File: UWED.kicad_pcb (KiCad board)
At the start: 2 copper layers, 34 x 49.5 mm, 52 parts, among them U1 RFD22301

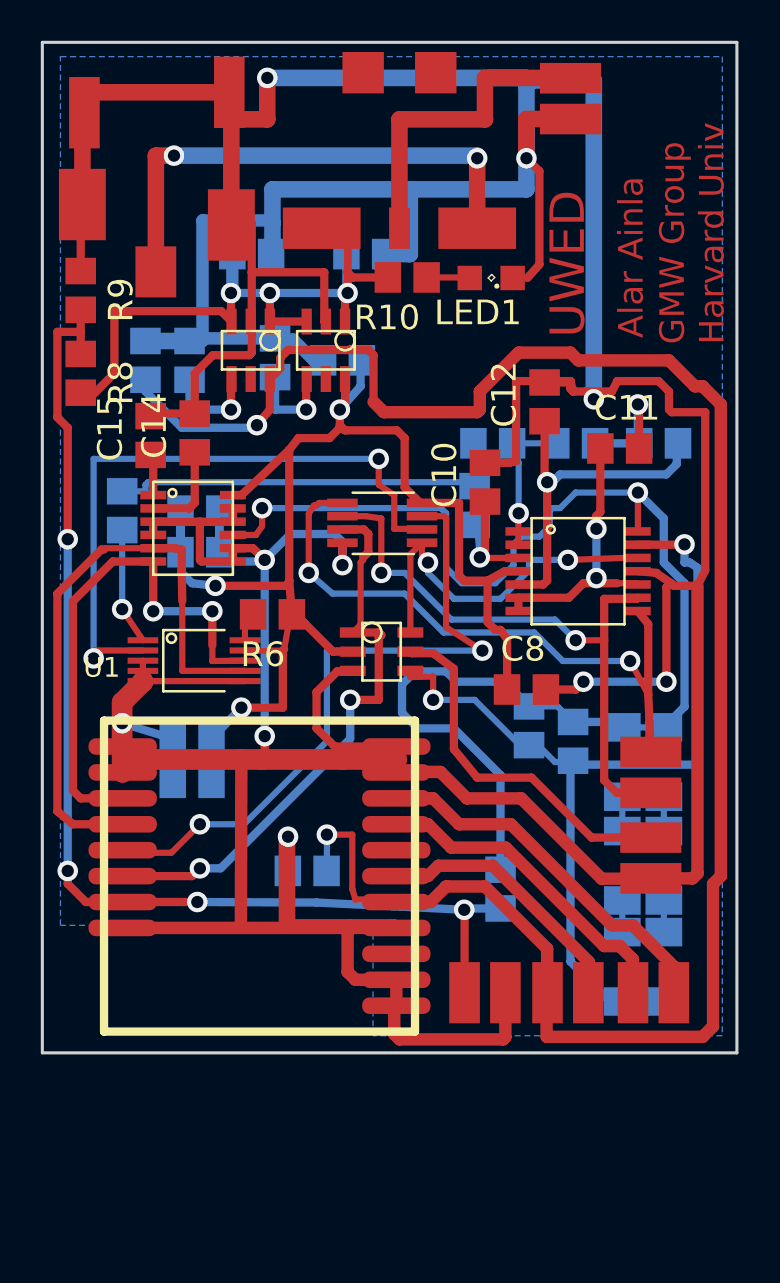
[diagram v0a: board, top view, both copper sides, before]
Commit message: New project files with ESP-WROOM-32 and integrated charger chip - untested.
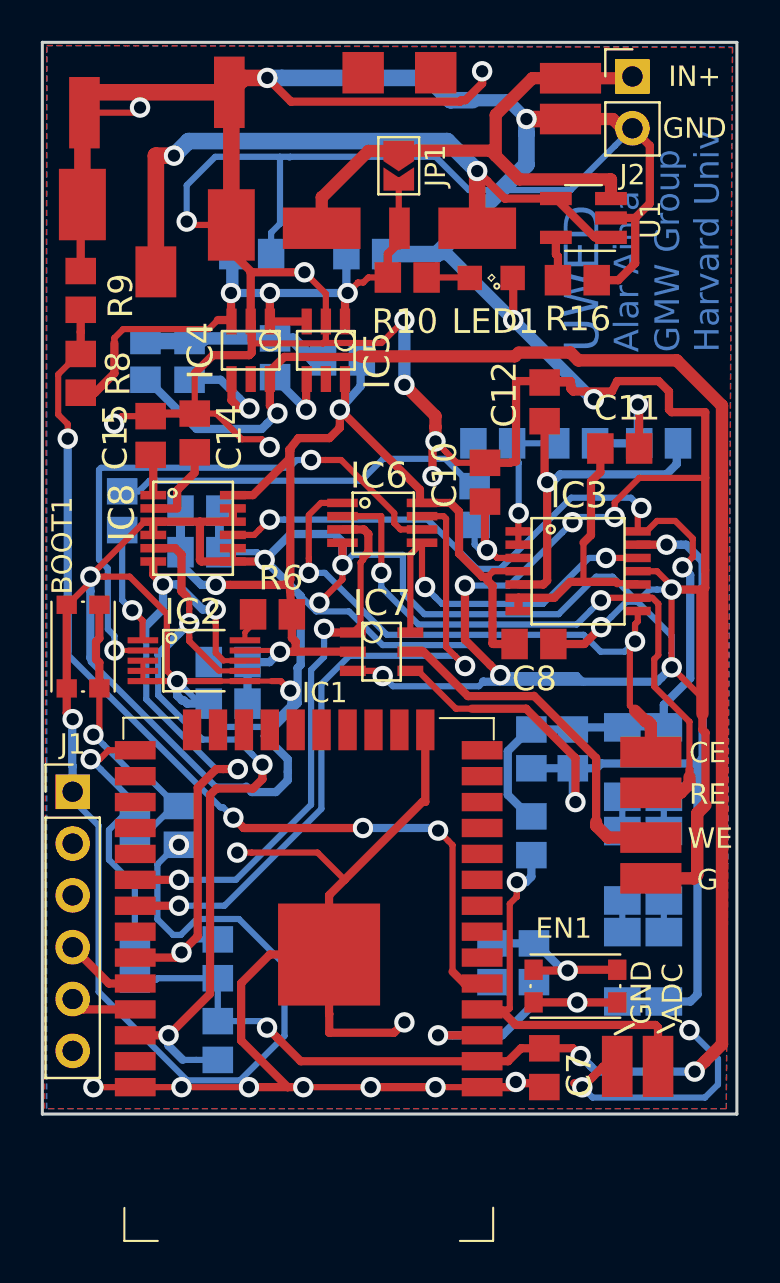
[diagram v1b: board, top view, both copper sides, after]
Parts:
- removed U$1: 4OPAMPS-AD8608ARUZ, UWED:MSOP14_0.65MM
- removed U$10, U$11: LDO-MIC5205-3.3YM5-TR, UWED:SOT-23-6
- removed U$12: SWITCH_MAX4643EUA, UWED:MSOP8_0.65MM
- removed U$13: SWITCH_MAX4644EUT, UWED:SOT-23-6
- removed U$14: SW_TOGGLELARGE, UWED:TOGGLE_34E
- removed U$2: ADC_LTC2471IMS, UWED:MSOP12_0.65MM
- removed U$4, U$5: CONTACT_PADS_SMD_2, UWED:CONTACT_PADS_SMD_2
- removed U$8: DAC_AD5667RBRMZ-2, UWED:MSOP10_0.5MM
- removed U$9: DC_JACK_0.7MM, UWED:PJ-032H-SMT
- added BOOT1: KMR221G LFS, Buttons_Switches_SMD:SW_SPST_KMR2, F.Cu at (133.5, 109.9)
- added C20: 1n, UWED:C0805, B.Cu at (138.2, 118.6)
- added C21: 1n, UWED:C0805, B.Cu at (153.5, 125.3)
- added EN1: KMR221G LFS, Buttons_Switches_SMD:SW_SPST_KMR2, F.Cu at (157.6, 126.5)
- added IC1: ESP32-WROOM-32, digikey-footprints:ESP32-WROOM-32D, F.Cu at (144.5, 123.2)
- added IC2: DAC_AD5667RBRMZ-2, UWED:MSOP10_0.5MM, F.Cu at (136.4, 109.5)
- added IC3: 4OPAMPS-AD8608ARUZ, UWED:MSOP14_0.65MM, F.Cu at (155.5, 104.2)
- added IC4: LDO-MIC5205-3.3YM5-TR, UWED:SOT-23-6, F.Cu at (142.6, 93.9)
- added IC5: LDO-MIC5205-3.3YM5-TR, UWED:SOT-23-6, F.Cu at (146.3, 93.9)
- added IC6: SWITCH_MAX4643EUA, UWED:MSOP8_0.65MM, F.Cu at (146.2, 102.8)
- added IC7: SWITCH_MAX4644EUT, UWED:SOT-23-6, F.Cu at (146.7, 109.2)
- added IC8: ADC_LTC2471IMS, UWED:MSOP12_0.65MM, F.Cu at (136.9, 102.4)
- added J1: DNP, Pin_Headers:Pin_Header_Straight_1x06_Pitch2.54mm, F.Cu at (133.0, 117.0)
- added J2: DNP, Pin_Headers:Pin_Header_Straight_1x02_Pitch2.54mm, F.Cu at (160.4, 81.9)
- added JP1: Jumper_2_Open, Jumper:SolderJumper-2_P1.3mm_Open_TrianglePad1.0x1.5mm, F.Cu at (148.9, 86.3)
- added P1: PJ-032H-SMT-TR, UWED:PJ-032H-SMT, F.Cu at (137.0, 79.2)
- added P2: 34EWMSP12M6RT, UWED:TOGGLE_34E, F.Cu at (147.2, 81.7)
- added R11: 10k, UWED:R0805, B.Cu at (140.1, 125.2)
- added R12: 10k, UWED:R0805, B.Cu at (140.1, 129.2)
- added R13: 100k, UWED:R0805, B.Cu at (136.0, 125.2)
- added R14: 470R, UWED:R0805, B.Cu at (136.0, 118.6)
- added R15: 470R, UWED:R0805, B.Cu at (155.6, 125.3)
- added R16: 4K7, UWED:R0805, F.Cu at (157.7, 91.9)
- C1, C16, C18, C2, C5, C6: value C-USC0805 -> 10u
- C10, C12: value C-USC0805 -> 10n
- C11, C13, C14, C15, C17, C19, C8, C9: value C-USC0805 -> 100n
- C3, C4: value C-USC0805 -> 470p
- C7: value C-USC0805 -> 100n; moved to F.Cu
- D1, D2, D3, D4, D5, D6: value PMLL4150 -> DNP
- LED1: value LEDSML0805 -> LED (blue)
- R1: value R-US_R0805 -> 1k2
- R10, R3: value R-US_R0805 -> 845R
- R2: value R-US_R0805 -> 16k2
- R4: value R-US_R0805 -> 29k4
- R5: value R-US_R0805 -> 8k6
- R6: value R-US_R0805 -> DNP
- R7: value R-US_R0805 -> OR
- R8, R9: value R-US_R0805 -> 100k
- U1: value RFD22301 -> MCP73812T-420I-OT; footprint UWED:RFD22301 -> TO_SOT_Packages_SMD:SOT-23-5_HandSoldering
- moved U1 37.1 mm to (158.0, 88.8), turned to 180 degrees
- moved C7 15.1 mm to (156.1, 130.5), turned to 270 degrees
- moved U$15 8.31 mm to (160.7, 130.4), turned to 0 degrees
- moved C17 4.26 mm to (140.6, 112.6)
- moved C16 4.15 mm to (140.6, 110.6)
- moved R7 3.02 mm to (155.4, 119.1)
- moved C8 2.26 mm to (155.6, 109.7)
- moved C13 1.14 mm to (155.4, 114.9)
- moved R5 0.37 mm to (157.5, 114.9)
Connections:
- net Net-(C13-Pad1) renamed /SIG-
- net Net-(C13-Pad2) renamed /OPA_OUT
- net Net-(C16-Pad1) renamed +3.3VA
- C5 pad 1: Net-(C5-Pad1) -> +3V3
- C7 pad 1: Net-(C5-Pad1) -> +3V3
- R7 pad 2: Net-(R7-Pad2) -> /ADCIn
- R8 pad 1: Net-(R7-Pad2) -> /BatIn
- R9 pad 2: Net-(R7-Pad2) -> /BatIn
- U$15 pad P$2: Net-(R7-Pad2) -> /ADCIn
- U$3 pad P$1: Net-(U$14-PadCOM) -> /PWR+
- U$6 pad P$1: Net-(U$13-PadP$5) -> /WE
- U$7 pad P$1: Net-(U$1-PadP$9) -> /RE
- U$7 pad P$2: Net-(U$1-PadP$8) -> /CE
- U1 pad 1: GND -> Net-(P1-Pad1)
- U1 pad 3: Net-(U$2-PadP$6) -> /PWR+
- U1 pad 4: Net-(U$2-PadP$5) -> Net-(P1-Pad1)
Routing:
- net GND: track 337.6 -> 543.2 mm, vias 10 -> 42
- net Net-(C5-Pad1): track 98.4 -> 0.00 mm, vias 2 -> 0
- net +3V3: track 0.00 -> 98.1 mm, vias 0 -> 4
- net Net-(R7-Pad2): track 56.3 -> 0.00 mm, vias 4 -> 0
- net /BatIn: track 0.00 -> 48.2 mm, vias 0 -> 4
- net /SCL: track 0.00 -> 41.0 mm, vias 0 -> 3
- net /SDA: track 0.00 -> 35.2 mm, vias 0 -> 4
- net /SwitchEl: track 0.00 -> 33.9 mm, vias 0 -> 2
- net /RE: track 0.00 -> 33.2 mm, vias 0 -> 2
- net Net-(P1-Pad1): track 0.00 -> 33.1 mm, vias 0 -> 2
- net Net-(U$12-PadP$6): track 31.8 -> 0.00 mm, vias 2 -> 0
- net /CE: track 0.00 -> 31.7 mm, vias 0 -> 2
- net Net-(U$1-PadP$8): track 31.3 -> 0.00 mm, vias 2 -> 0
- net Net-(R16-Pad1): track 33.1 -> 2.14 mm, vias 2 -> 0
- net Net-(U$2-PadP$5): track 30.1 -> 0.00 mm
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- added copper zone on F.Cu, net GND
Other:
- board size 34 x 49.5 mm -> 34 x 52.5 mm
- net class Default: clearance 0.1778 -> 0.2; trace_width 0.25 -> 0.305; via_dia 0.8 -> 1; via_drill 0.4 -> 0.6
- rule pad_to_mask_clearance: 0 -> 0.05
- rule solder_mask_min_width: 0.25 -> 0.15
- rule trace_clearance: 0.1778 -> 0.2
- rule trace_min: 0.2 -> 0.25
- rule via_min_size: 0.4 -> 0.6
- board text added: "ADC"
- board text added: "CE"
- board text added: "G"
- board text added: "GND"
- board text added: "IN+"
- board text added: "RE"
- board text added: "WE"
